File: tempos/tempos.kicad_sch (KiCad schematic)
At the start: 7 parts, among them SW1 SW_Push, SW2 SW_Push, U1 WeMos_D1_mini, U2 74HC595, U3 MAX3485, U4 CD4052B

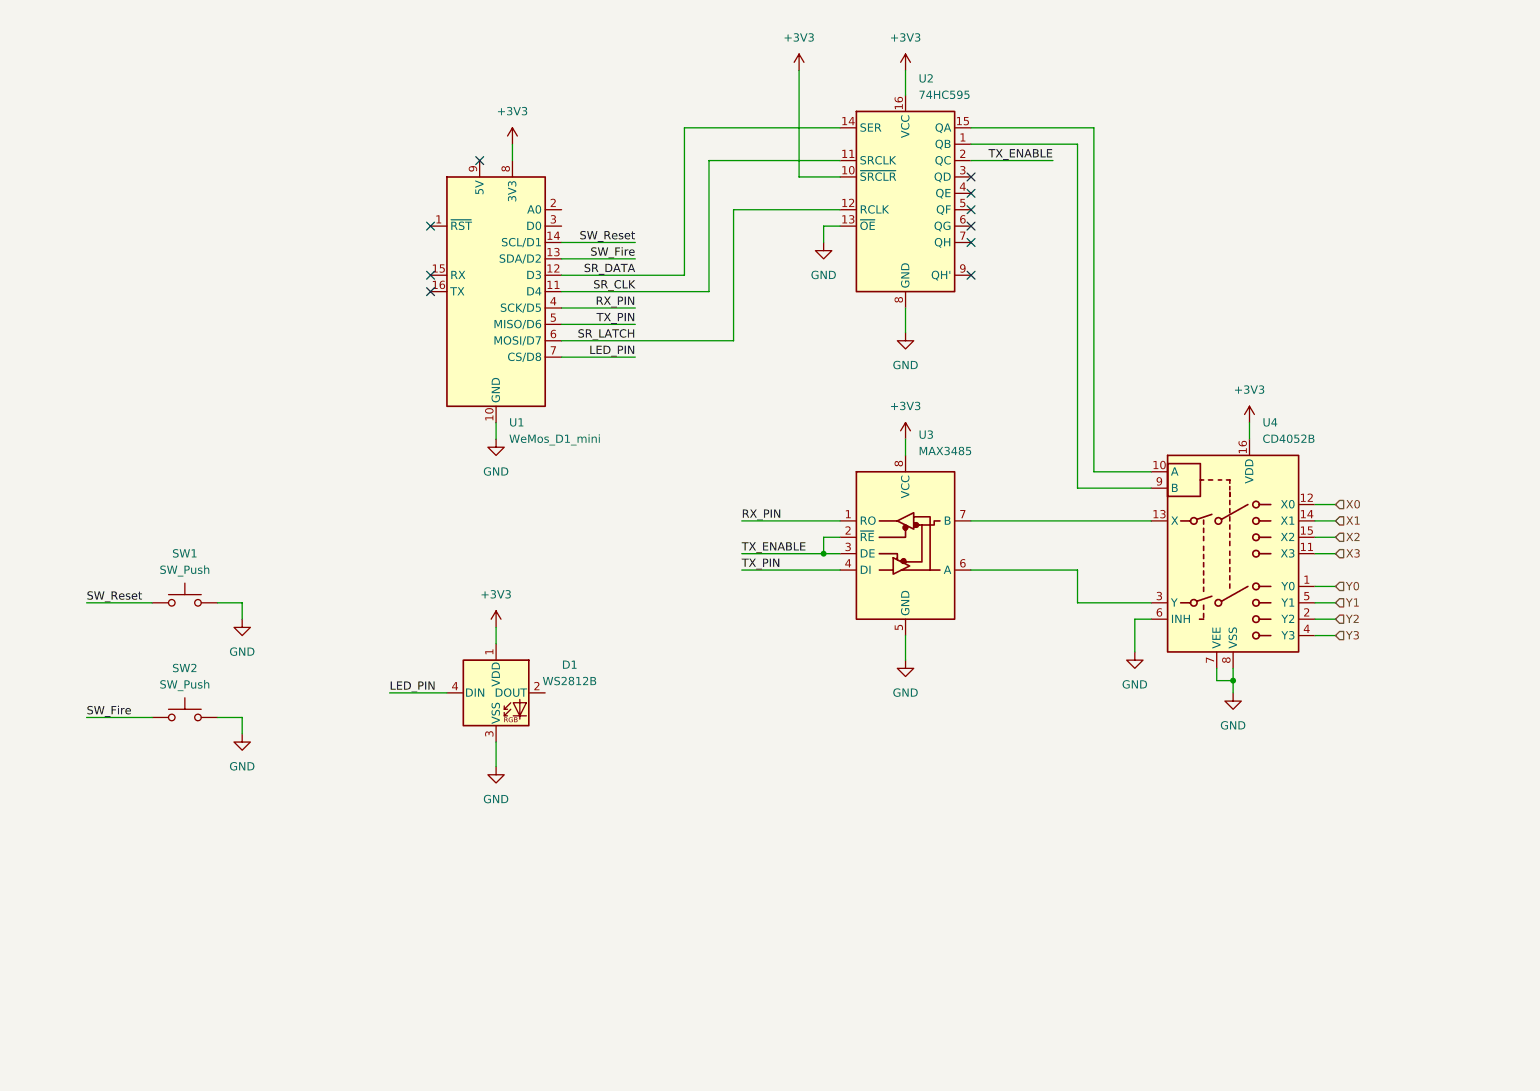
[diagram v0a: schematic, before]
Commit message: tempos: Alignment in schematics to grid: 2.54
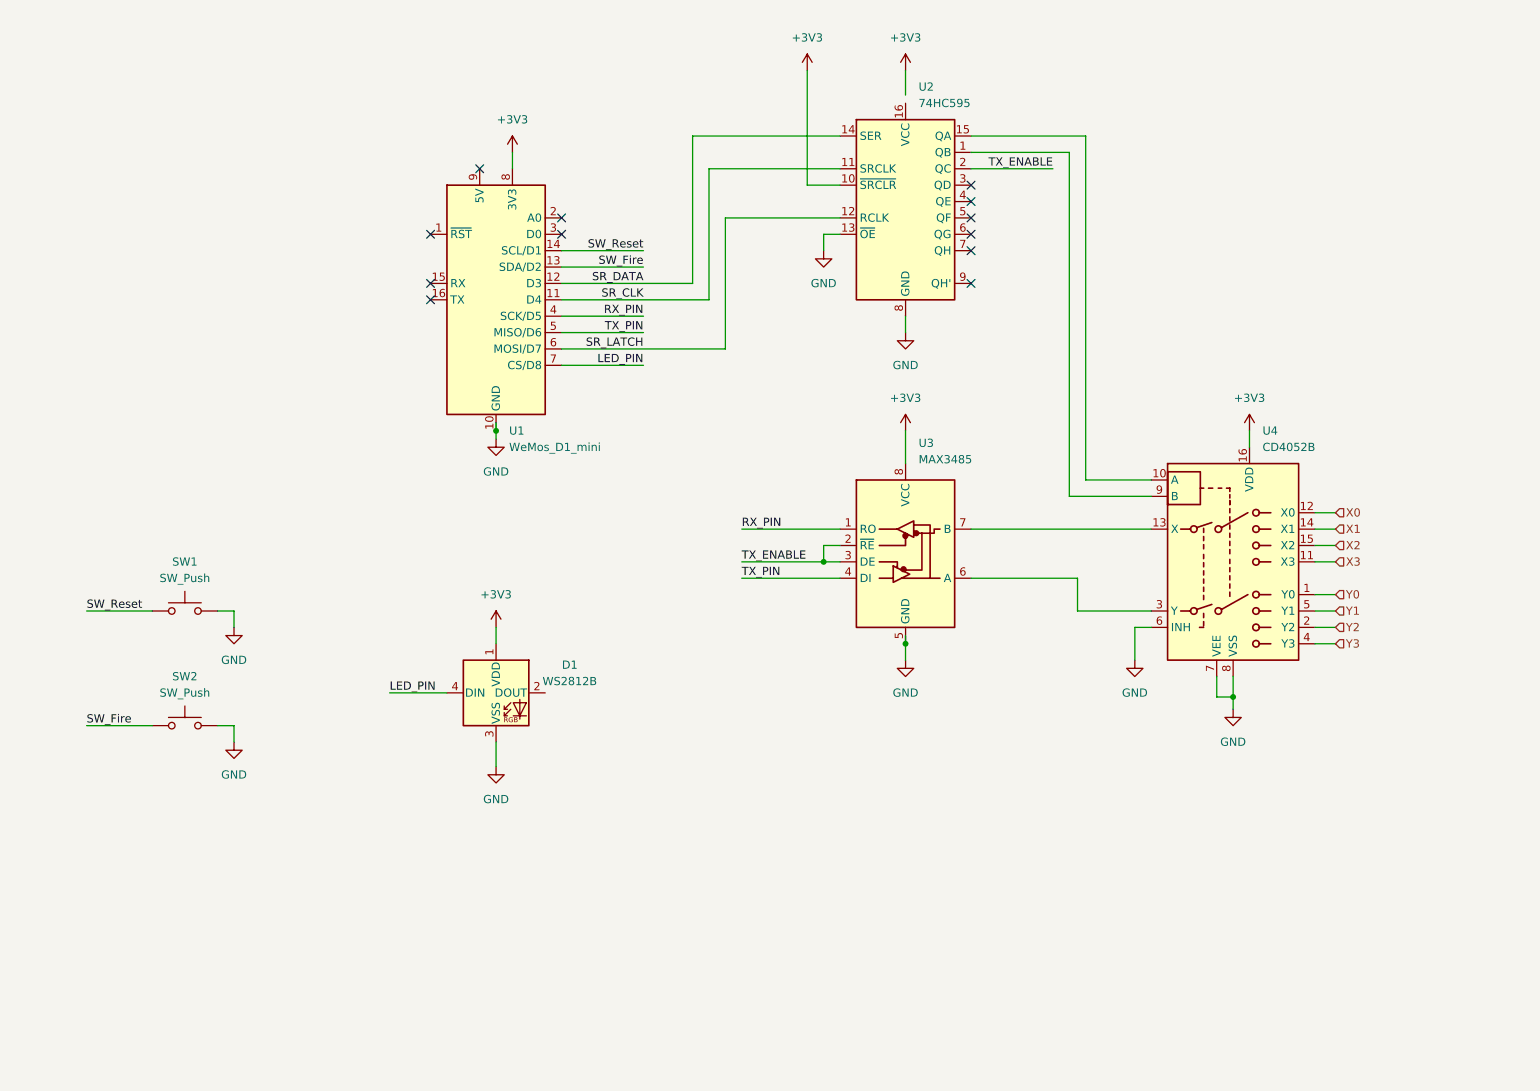
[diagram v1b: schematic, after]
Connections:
- net +3V3: no longer U2.16 (VCC)
- no-connect marks 10 -> 12
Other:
- moved on the sheet: SW1, SW2, U1, U2, U3, U4

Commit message: tempos: Include more LEDs in schematics
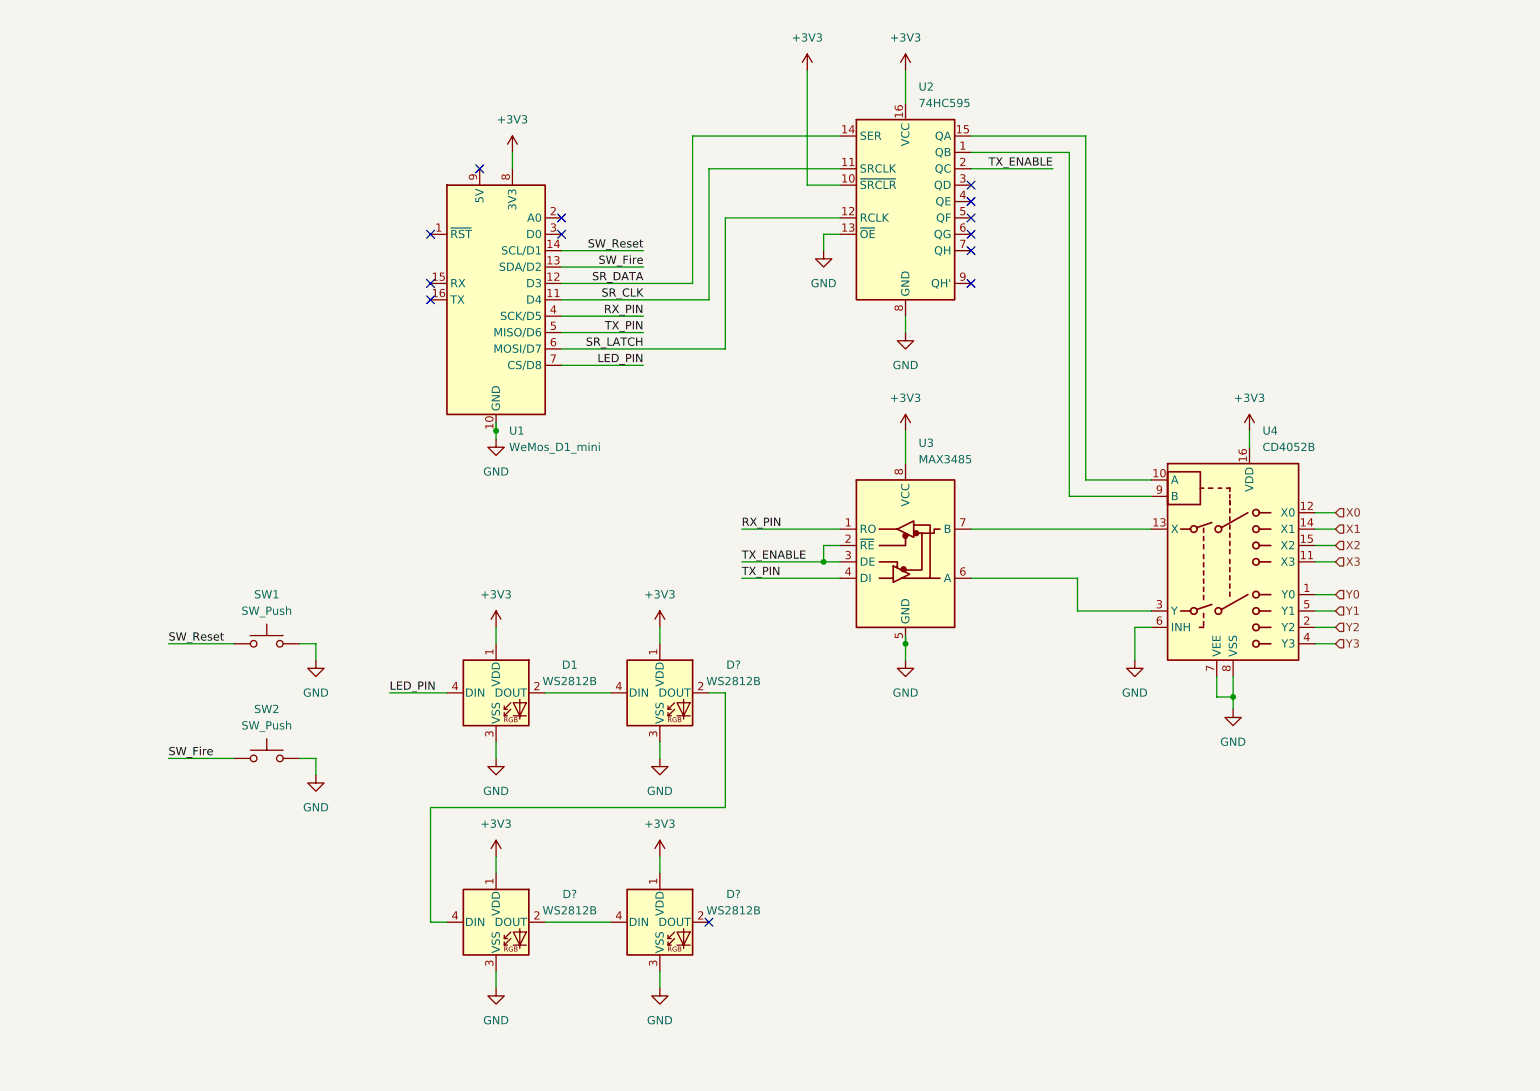
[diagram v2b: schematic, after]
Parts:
- added D? (x3): WS2812B, symbol tempos:WS2812B
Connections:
- net +3V3: now also U2.16 (VCC), D?.1 (VDD), D?.1 (VDD), D?.1 (VDD)
- net GND: now also D?.3 (VSS), D?.3 (VSS), D?.3 (VSS)
- net at D1.2 (DOUT): now also D?.4 (DIN)
- new net: D?.2 (DOUT), D?.4 (DIN) (x2)
- no-connect marks 12 -> 13
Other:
- moved on the sheet: SW1, SW2

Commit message: tempos: DIP switch for hardware configuration
8 channel multiplexer to add more configuration mode for the hardware.
We're using 2 switches for setting off a fire and reseting the node.
There's also a DIP switch for configuring the node as an exit.
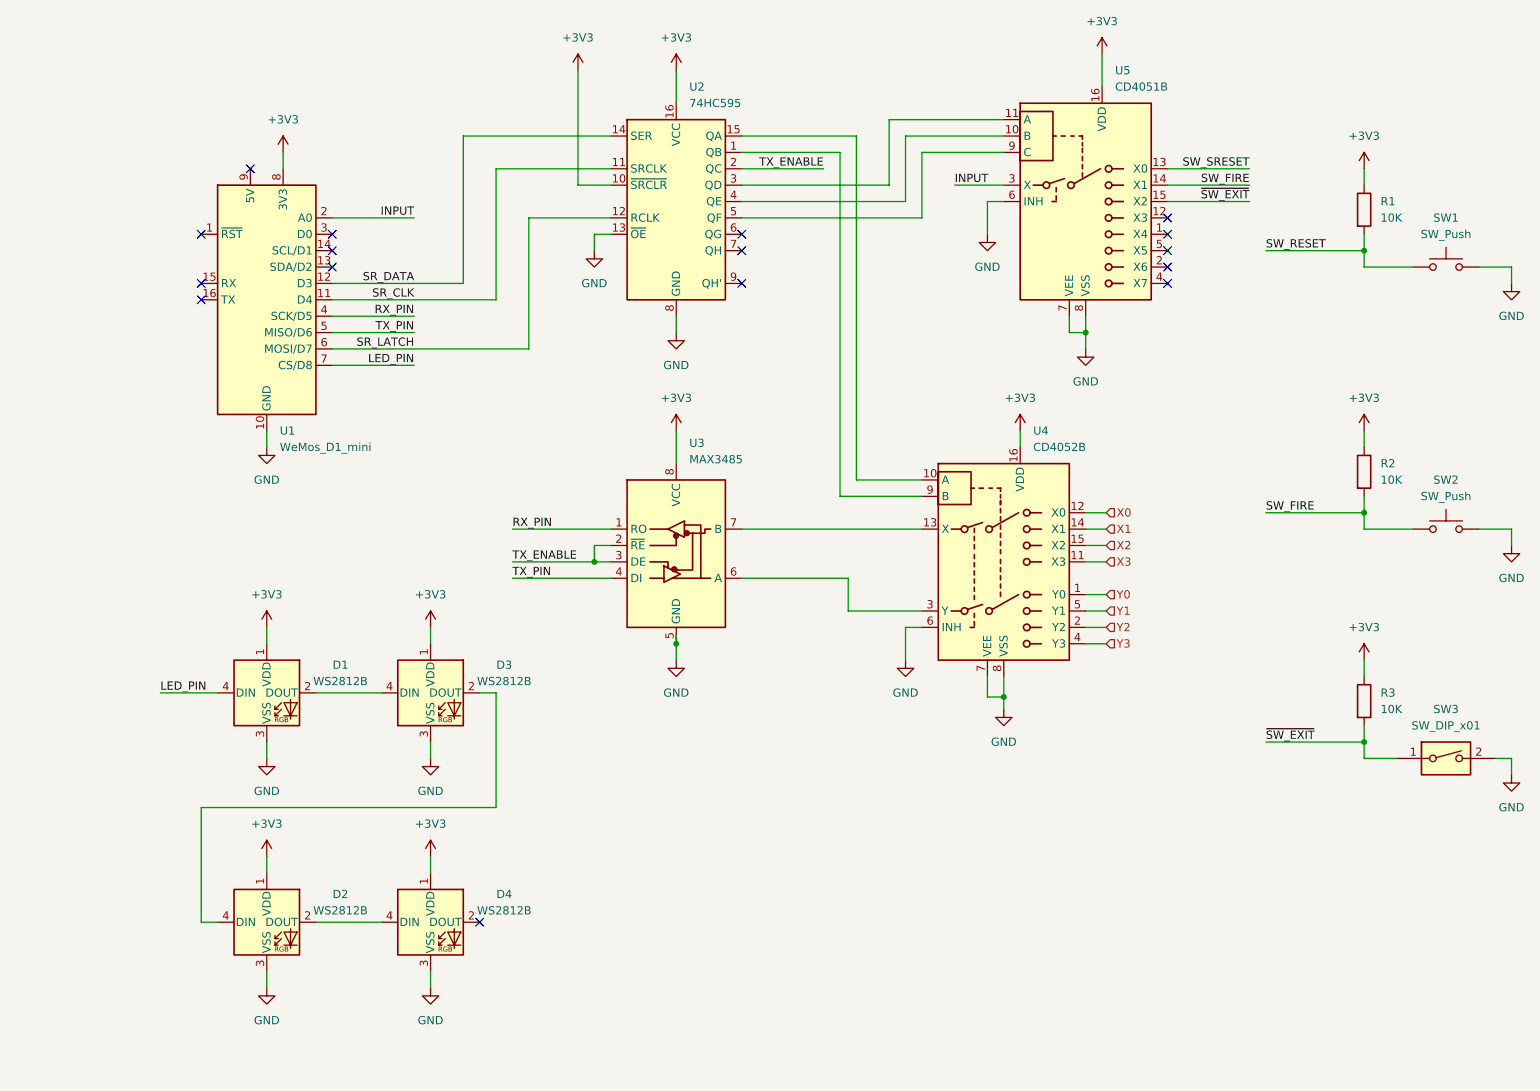
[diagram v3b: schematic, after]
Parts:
- added R1, R2, R3: 10K, symbol Device:R
- added SW3: SW_DIP_x01, symbol Switch:SW_DIP_x01
- added U5: CD4051B, symbol Analog_Switch:CD4051B
- gave numbers to parts that had none: 3
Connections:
- net +3V3: now also R1.1, R2.1, R3.1, U5.16 (VDD)
- net GND: now also SW3.2, U5.6 (INH), U5.7 (VEE), U5.8 (VSS)
- net at U2.3 (QD): now also U5.11 (A)
- net at U2.4 (QE): now also U5.10 (B)
- net at U2.5 (QF): now also U5.9 (C)
- net INPUT: now reaches U1.2 (A0)
- net INPUT: now also U5.3 (X)
- net SW_Fire: no longer names the net of U1.13 (SDA/D2)
- net SW_Fire: no longer SW2.1
- net SW_Reset: no longer names the net of U1.14 (SCL/D1)
- net SW_Reset: no longer SW1.1
- new net SW_FIRE: R2.2, SW2.1, U5.14 (X1)
- new net SW_RESET: R1.2, SW1.1
- new net SW_SRESET: U5.13 (X0)
- new net ~{SW_EXIT}: R3.2, SW3.1, U5.15 (X2)
- no-connect marks 13 -> 16
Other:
- moved on the sheet: D1, D2, D3, D4, SW1, U1, U2, U3, U4

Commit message: tempos+sunlight: Full duplex communication
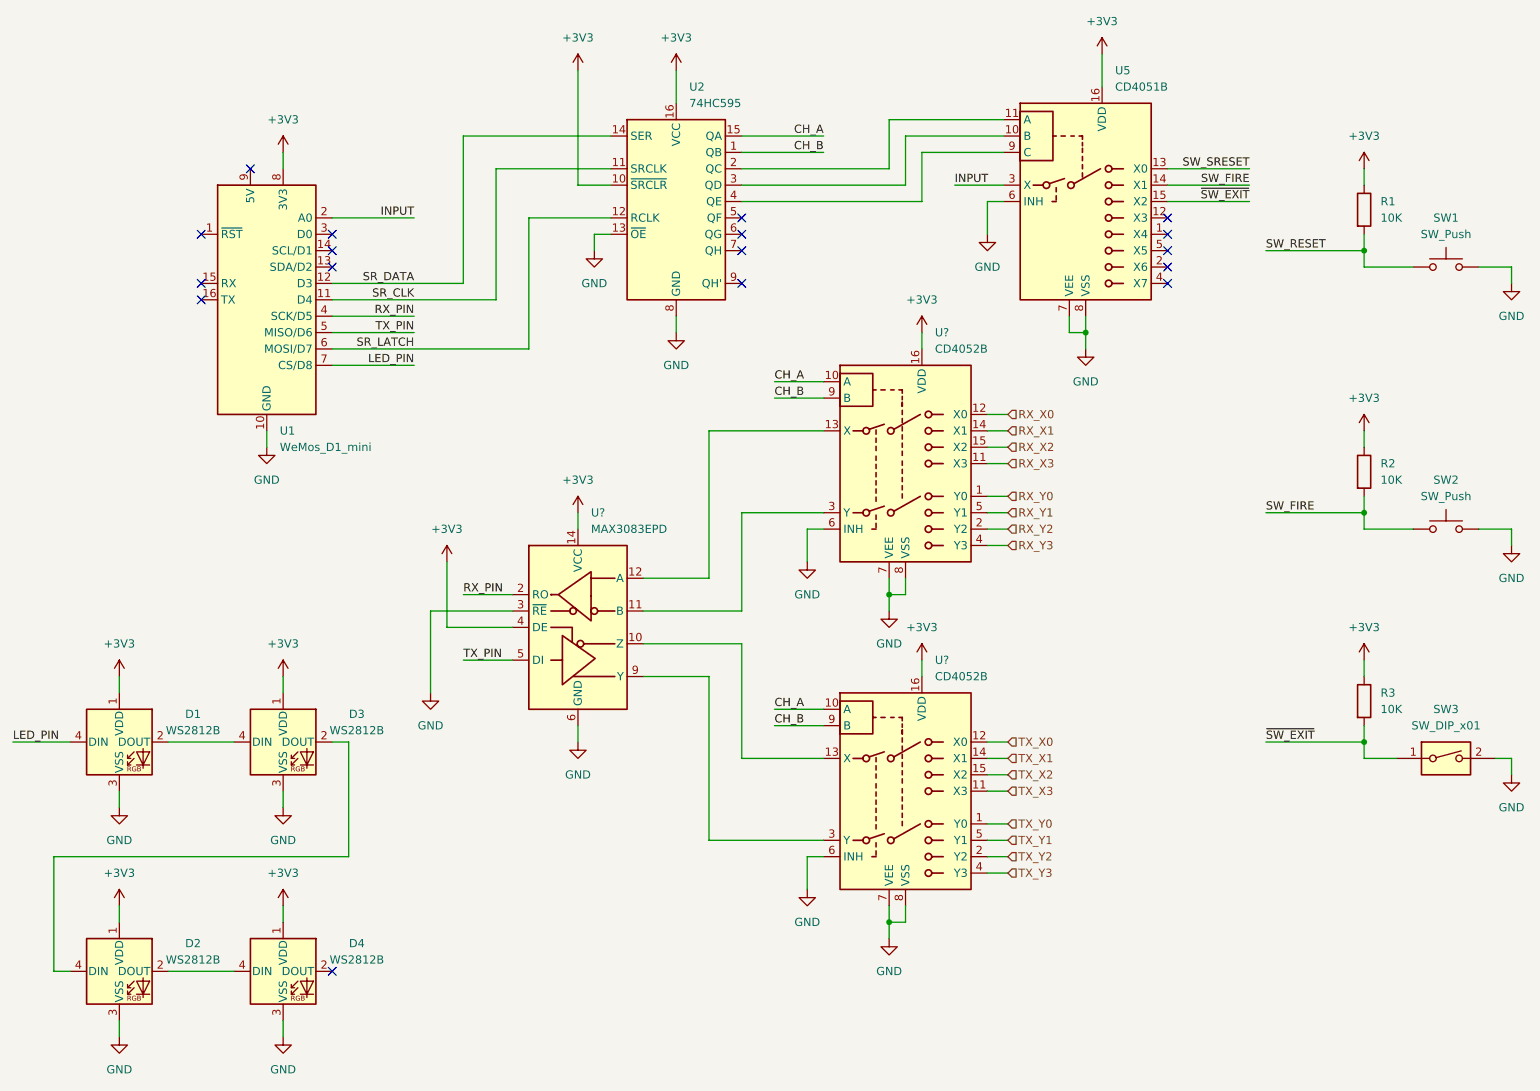
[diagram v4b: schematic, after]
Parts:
- removed U3: MAX3485, symbol Interface_UART:MAX3485
- removed U4: CD4052B, symbol Analog_Switch:CD4052B
- added U? (x2): CD4052B, symbol Analog_Switch:CD4052B
- added U?: MAX3083EPD, Package_DIP:DIP-14_W7.62mm, symbol tempos:MAX3083EPD
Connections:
- net TX_ENABLE is gone; now on an unnamed net: U2.2 (QC)
- net +3V3: now also U?.14 (VCC), U?.16 (VDD), U?.16 (VDD), U?.4 (DE)
- net GND: now also U?.3 (~{RE}), U?.6 (GND), U?.6 (INH), U?.6 (INH), U?.7 (GND), U?.7 (VEE), U?.7 (VEE), U?.8 (VSS), U?.8 (VSS)
- net RX_PIN: now also U?.2 (RO)
- net TX_PIN: now also U?.5 (DI)
- net at U5.10 (B): now also U2.3 (QD); no longer U2.4 (QE)
- net at U5.11 (A): no longer U2.3 (QD)
- net at U5.9 (C): now also U2.4 (QE); no longer U2.5 (QF)
- net CH_B: now reaches U2.1 (QB)
- net CH_B: now also U?.9 (B), U?.9 (B)
- net CH_A: now reaches U2.15 (QA)
- net CH_A: now also U?.10 (A), U?.10 (A)
- new net: U?.10 (Z), U?.13 (X)
- new net: U?.3 (Y), U?.9 (Y)
- new net: U?.11 (B), U?.3 (Y)
- new net: U?.12 (A), U?.13 (X)
- new net RX_X0: U?.12 (X0)
- new net RX_X1: U?.14 (X1)
- new net RX_X2: U?.15 (X2)
- new net RX_X3: U?.11 (X3)
- new net RX_Y0: U?.1 (Y0)
- new net RX_Y1: U?.5 (Y1)
- new net RX_Y2: U?.2 (Y2)
- new net RX_Y3: U?.4 (Y3)
- new net TX_X0: U?.12 (X0)
- new net TX_X1: U?.14 (X1)
- new net TX_X2: U?.15 (X2)
- new net TX_X3: U?.11 (X3)
- new net TX_Y0: U?.1 (Y0)
- new net TX_Y1: U?.5 (Y1)
- new net TX_Y2: U?.2 (Y2)
- new net TX_Y3: U?.4 (Y3)
- no-connect marks 16 -> 17
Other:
- moved on the sheet: D1, D2, D3, D4
